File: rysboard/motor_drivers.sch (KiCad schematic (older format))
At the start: 30 parts, among them J2 Motor L, J3 Motor R, U1 L6470, U2 L6470, U5 74HC2G00

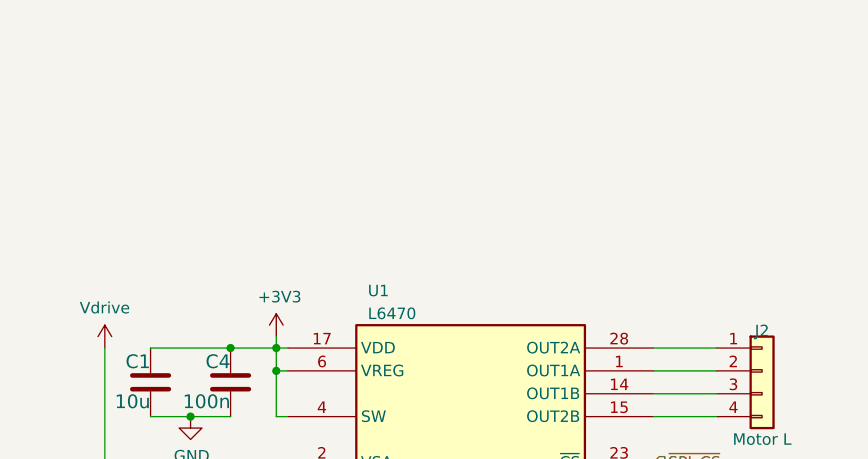
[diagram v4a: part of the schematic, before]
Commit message: first modyfications in St Motor section
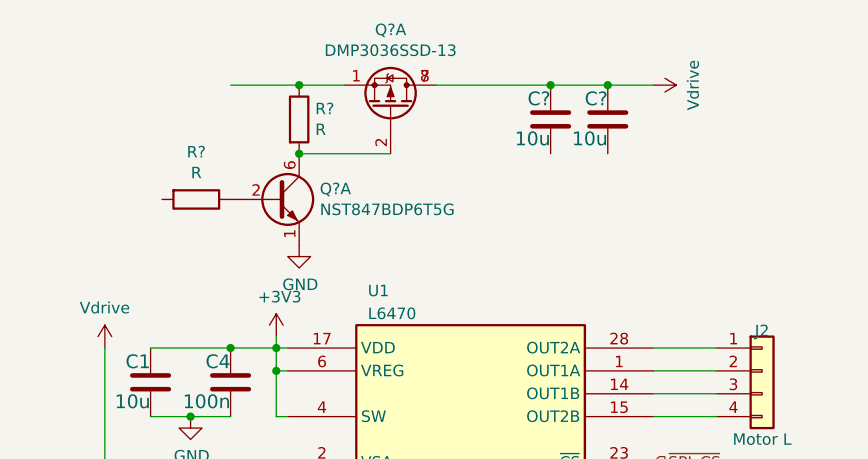
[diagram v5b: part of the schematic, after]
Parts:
- added C? (x2): 10u, Capacitor_SMD:C_1206_3216Metric, symbol Device:C
- added Q?: DMP3036SSD-13, Package_SO:SO-8_5.3x6.2mm_P1.27mm, symbol rysboard:DMP3036SSD-13
- added Q?: NST847BDP6T5G, Package_TO_SOT_SMD:SOT-963, symbol rysboard:NST847BDP6T5G
- added R? (x2): R, symbol Device:R
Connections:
- net GND: now also Q?.1 (E1)
- net Vdrive: now also C?.1, C?.1, Q?.7 (d), Q?.8 (d)
- new net: Q?.1 (S1), R?.1
- new net: Q?.2 (G1), Q?.6 (C1), R?.2
- new net: Q?.2 (B1), R?.1
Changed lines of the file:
@@
 	1    0    0    -1
 $EndComp
+$Comp
+L rysboard:DMP3036SSD-13 Q?
+U 1 1 603966B2
+P 2900 1050
+F 0 "Q?" V 3242 1050 50  0000 C CNN
+F 1 "DMP3036SSD-13" V 3151 1050 50  0000 C CNN
+F 2 "Package_SO:SO-8_5.3x6.2mm_P1.27mm" H 3100 975 50  0001 L CIN
+F 3 "http://www.vishay.com/docs/70209/70209.pdf" H 2900 1050 50  0001 L CNN
+	1    2900 1050
+	0    1    -1   0
+$EndComp
+$Comp
+L Device:C C?
+U 1 1 603970BA
+P 3600 1100
+F 0 "C?" H 3600 1225 60  0000 R TNN
+F 1 "10u" H 3600 1050 60  0000 R TNN
+F 2 "Capacitor_SMD:C_1206_3216Metric" H 3500 1190 60  0001 C CNN
+F 3 "" H 3500 1190 60  0000 C CNN
+	1    3600 1100
+	1    0    0    -1
+$EndComp
+$Comp
+L Device:C C?
+U 1 1 60397388
+P 3850 1100
+F 0 "C?" H 3850 1225 60  0000 R TNN
+F 1 "10u" H 3850 1050 60  0000 R TNN
+F 2 "Capacitor_SMD:C_1206_3216Metric" H 3750 1190 60  0001 C CNN
+F 3 "" H 3750 1190 60  0000 C CNN
+	1    3850 1100
+	1    0    0    -1
+$EndComp
+Wire Wire Line
+	3100 950  3600 950
+Connection ~ 3600 950
+Wire Wire Line
+	3600 950  3850 950
+$Comp
+L power:Vdrive #PWR?
+U 1 1 6039DE74
+P 4050 950
+F 0 "#PWR?" H 3850 800 50  0001 C CNN
+F 1 "Vdrive" H 4050 1125 50  0000 C CNN
+F 2 "" H 4050 950 50  0001 C CNN
+F 3 "" H 4050 950 50  0001 C CNN
+	1    4050 950
+	0    1    1    0
+$EndComp
+Wire Wire Line
+	4050 950  3850 950
+Connection ~ 3850 950
+$Comp
+L rysboard:NST847BDP6T5G Q?
+U 1 1 603A44DC
+P 2400 1450
+F 0 "Q?" H 2590 1496 50  0000 L CNN
+F 1 "NST847BDP6T5G" H 2590 1405 50  0000 L CNN
+F 2 "Package_TO_SOT_SMD:SOT-963" H 2600 1550 50  0001 C CNN
+F 3 "~" H 2400 1450 50  0001 C CNN
+	1    2400 1450
+	1    0    0    -1
+$EndComp
+$Comp
+L power:GND #PWR?
+U 1 1 603A5682
+P 2500 1650
+F 0 "#PWR?" H 2500 1400 50  0001 C CNN
+F 1 "GND" H 2505 1477 50  0000 C CNN
+F 2 "" H 2500 1650 50  0001 C CNN
+F 3 "" H 2500 1650 50  0001 C CNN
+	1    2500 1650
+	1    0    0    -1
+$EndComp
+Wire Wire Line
+	2500 1250 2900 1250
+$Comp
+L Device:R R?
+U 1 1 603AB9BC
+P 2500 1100
+F 0 "R?" H 2570 1146 50  0000 L CNN
+F 1 "R" H 2570 1055 50  0000 L CNN
+F 2 "" V 2430 1100 50  0001 C CNN
+F 3 "~" H 2500 1100 50  0001 C CNN
+	1    2500 1100
+	1    0    0    -1
+$EndComp
+Connection ~ 2500 1250
+Wire Wire Line
+	2700 950  2500 950
+Connection ~ 2500 950
+Wire Wire Line
+	2500 950  2200 950
+$Comp
+L Device:R R?
+U 1 1 603B1D08
+P 2050 1450
+F 0 "R?" V 1843 1450 50  0000 C CNN
+F 1 "R" V 1934 1450 50  0000 C CNN
+F 2 "" V 1980 1450 50  0001 C CNN
+F 3 "~" H 2050 1450 50  0001 C CNN
+	1    2050 1450
+	0    1    1    0
+$EndComp
 $EndSCHEMATC

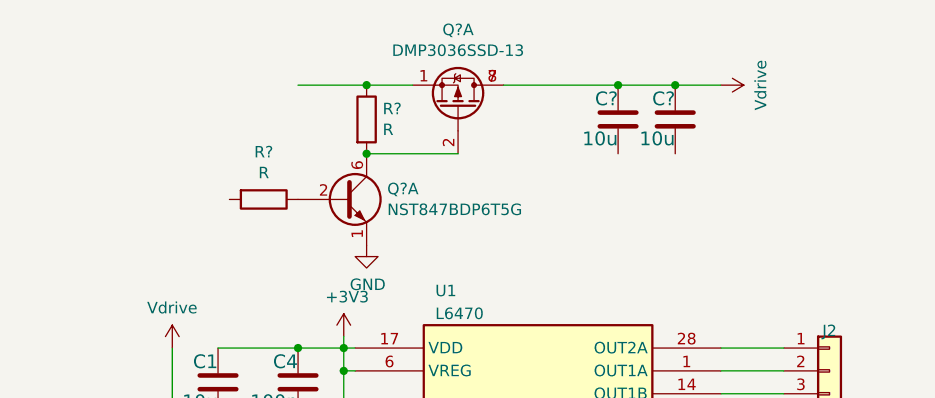
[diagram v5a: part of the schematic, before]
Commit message: Added eval board for STM32G031K8U6, rybsoard layout done, exact vals yet to be calculated
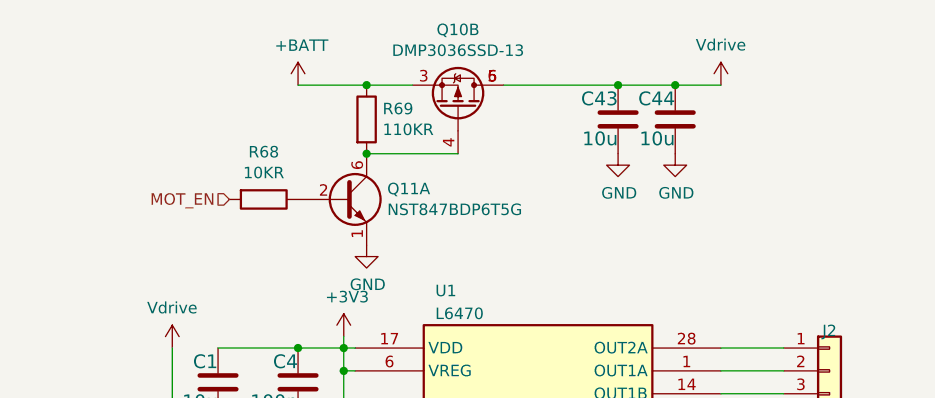
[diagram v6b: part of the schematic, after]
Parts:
- R68: renamed from R?; value R -> 10KR
- R69: renamed from R?; value R -> 110KR
- gave numbers to parts that had none: 4
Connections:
- net GND: now also C43.2, C44.2
- net Vdrive: now also Q10.5 (d), Q10.6 (d); no longer Q10.7 (d), Q10.8 (d)
- net +BATT: now reaches R69.1
- net +BATT: now also Q10.3 (S2); no longer Q10.1 (S1)
- net at Q11.6 (C1), R69.2: now also Q10.4 (G2); no longer Q10.2 (G1)
- net MOT_EN: now reaches R68.2
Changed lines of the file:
@@
 $Descr A4 11693 8268
 encoding utf-8
-Sheet 6 7
+Sheet 7 7
 Title "rysboard"
 Date "2020-08-23"
@@
 $EndComp
 $Comp
-L rysboard:DMP3036SSD-13 Q?
-U 1 1 603966B2
+L rysboard:DMP3036SSD-13 Q10
+U 2 1 603966B2
 P 2900 1050
-F 0 "Q?" V 3242 1050 50  0000 C CNN
+F 0 "Q10" V 3242 1050 50  0000 C CNN
 F 1 "DMP3036SSD-13" V 3151 1050 50  0000 C CNN
 F 2 "Package_SO:SO-8_5.3x6.2mm_P1.27mm" H 3100 975 50  0001 L CIN
 F 3 "http://www.vishay.com/docs/70209/70209.pdf" H 2900 1050 50  0001 L CNN
-	1    2900 1050
+	2    2900 1050
 	0    1    -1   0
 $EndComp
 $Comp
-L Device:C C?
+L Device:C C43
 U 1 1 603970BA
 P 3600 1100
-F 0 "C?" H 3600 1225 60  0000 R TNN
+F 0 "C43" H 3600 1225 60  0000 R TNN
 F 1 "10u" H 3600 1050 60  0000 R TNN
 F 2 "Capacitor_SMD:C_1206_3216Metric" H 3500 1190 60  0001 C CNN
@@
 $EndComp
 $Comp
-L Device:C C?
+L Device:C C44
 U 1 1 60397388
 P 3850 1100
-F 0 "C?" H 3850 1225 60  0000 R TNN
+F 0 "C44" H 3850 1225 60  0000 R TNN
 F 1 "10u" H 3850 1050 60  0000 R TNN
 F 2 "Capacitor_SMD:C_1206_3216Metric" H 3750 1190 60  0001 C CNN
@@
 	3600 950  3850 950
 $Comp
-L power:Vdrive #PWR?
+L power:Vdrive #PWR059
 U 1 1 6039DE74
 P 4050 950
-F 0 "#PWR?" H 3850 800 50  0001 C CNN
+F 0 "#PWR059" H 3850 800 50  0001 C CNN
 F 1 "Vdrive" H 4050 1125 50  0000 C CNN
 F 2 "" H 4050 950 50  0001 C CNN
 F 3 "" H 4050 950 50  0001 C CNN
 	1    4050 950
-	0    1    1    0
+	1    0    0    -1
 $EndComp
 Wire Wire Line
@@
 Connection ~ 3850 950
 $Comp
-L rysboard:NST847BDP6T5G Q?
+L rysboard:NST847BDP6T5G Q11
 U 1 1 603A44DC
 P 2400 1450
-F 0 "Q?" H 2590 1496 50  0000 L CNN
+F 0 "Q11" H 2590 1496 50  0000 L CNN
 F 1 "NST847BDP6T5G" H 2590 1405 50  0000 L CNN
 F 2 "Package_TO_SOT_SMD:SOT-963" H 2600 1550 50  0001 C CNN
@@
 $EndComp
 $Comp
-L power:GND #PWR?
+L power:GND #PWR058
 U 1 1 603A5682
 P 2500 1650
-F 0 "#PWR?" H 2500 1400 50  0001 C CNN
+F 0 "#PWR058" H 2500 1400 50  0001 C CNN
 F 1 "GND" H 2505 1477 50  0000 C CNN
 F 2 "" H 2500 1650 50  0001 C CNN
@@
 	2500 1250 2900 1250
 $Comp
-L Device:R R?
+L Device:R R69
 U 1 1 603AB9BC
 P 2500 1100
-F 0 "R?" H 2570 1146 50  0000 L CNN
-F 1 "R" H 2570 1055 50  0000 L CNN
+F 0 "R69" H 2570 1146 50  0000 L CNN
+F 1 "110KR" H 2570 1055 50  0000 L CNN
 F 2 "" V 2430 1100 50  0001 C CNN
 F 3 "~" H 2500 1100 50  0001 C CNN
@@
 	2500 950  2200 950
 $Comp
-L Device:R R?
+L Device:R R68
 U 1 1 603B1D08
 P 2050 1450
-F 0 "R?" V 1843 1450 50  0000 C CNN
-F 1 "R" V 1934 1450 50  0000 C CNN
+F 0 "R68" V 1843 1450 50  0000 C CNN
+F 1 "10KR" V 1934 1450 50  0000 C CNN
 F 2 "" V 1980 1450 50  0001 C CNN
 F 3 "~" H 2050 1450 50  0001 C CNN
@@
 	0    1    1    0
 $EndComp
+Text HLabel 1900 1450 0    50   Input ~ 0
+MOT_EN
+$Comp
+L power:+BATT #PWR?
+U 1 1 6042D379
+P 2200 950
+F 0 "#PWR?" H 2200 800 50  0001 C CNN
+F 1 "+BATT" H 2215 1123 50  0000 C CNN
+F 2 "" H 2200 950 50  0001 C CNN
+F 3 "" H 2200 950 50  0001 C CNN
+	1    2200 950
+	1    0    0    -1
+$EndComp
+$Comp
+L power:GND #PWR?
+U 1 1 6042EE06
+P 3600 1250
+F 0 "#PWR?" H 3600 1000 50  0001 C CNN
+F 1 "GND" H 3605 1077 50  0000 C CNN
+F 2 "" H 3600 1250 50  0001 C CNN
+F 3 "" H 3600 1250 50  0001 C CNN
+	1    3600 1250
+	1    0    0    -1
+$EndComp
+$Comp
+L power:GND #PWR?
+U 1 1 6042F02D
+P 3850 1250
+F 0 "#PWR?" H 3850 1000 50  0001 C CNN
+F 1 "GND" H 3855 1077 50  0000 C CNN
+F 2 "" H 3850 1250 50  0001 C CNN
+F 3 "" H 3850 1250 50  0001 C CNN
+	1    3850 1250
+	1    0    0    -1
+$EndComp
 $EndSCHEMATC

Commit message: new mosfet footprints
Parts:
- R68, R69: footprint (none) -> Resistor_SMD:R_0603_1608Metric
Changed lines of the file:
@@
 F 0 "R69" H 2570 1146 50  0000 L CNN
 F 1 "110KR" H 2570 1055 50  0000 L CNN
-F 2 "" V 2430 1100 50  0001 C CNN
+F 2 "Resistor_SMD:R_0603_1608Metric" V 2430 1100 50  0001 C CNN
 F 3 "~" H 2500 1100 50  0001 C CNN
 	1    2500 1100
@@
 F 0 "R68" V 1843 1450 50  0000 C CNN
 F 1 "10KR" V 1934 1450 50  0000 C CNN
-F 2 "" V 1980 1450 50  0001 C CNN
+F 2 "Resistor_SMD:R_0603_1608Metric" V 1980 1450 50  0001 C CNN
 F 3 "~" H 2050 1450 50  0001 C CNN
 	1    2050 1450
@@
 MOT_EN
 $Comp
-L power:+BATT #PWR?
+L power:+BATT #PWR062
 U 1 1 6042D379
 P 2200 950
-F 0 "#PWR?" H 2200 800 50  0001 C CNN
+F 0 "#PWR062" H 2200 800 50  0001 C CNN
 F 1 "+BATT" H 2215 1123 50  0000 C CNN
 F 2 "" H 2200 950 50  0001 C CNN
@@
 $EndComp
 $Comp
-L power:GND #PWR?
+L power:GND #PWR063
 U 1 1 6042EE06
 P 3600 1250
-F 0 "#PWR?" H 3600 1000 50  0001 C CNN
+F 0 "#PWR063" H 3600 1000 50  0001 C CNN
 F 1 "GND" H 3605 1077 50  0000 C CNN
 F 2 "" H 3600 1250 50  0001 C CNN
@@
 $EndComp
 $Comp
-L power:GND #PWR?
+L power:GND #PWR064
 U 1 1 6042F02D
 P 3850 1250
-F 0 "#PWR?" H 3850 1000 50  0001 C CNN
+F 0 "#PWR064" H 3850 1000 50  0001 C CNN
 F 1 "GND" H 3855 1077 50  0000 C CNN
 F 2 "" H 3850 1250 50  0001 C CNN

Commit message: Fixed library, added a few MOSFET layouts
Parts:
- removed Q10: DMP3036SSD-13, Package_SO:SO-8_5.3x6.2mm_P1.27mm, symbol rysboard:DMP3036SSD-13
- added Q8: DMP3036SSD-13, Package_SO:SO-8_3.9x4.9mm_P1.27mm, symbol rysboard:DMP3036SSD-13
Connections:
- net +BATT: now also Q8.3 (S2)
- net Vdrive: now also Q8.5 (d), Q8.6 (d)
- net at Q11.6 (C1), R69.2: now also Q8.4 (G2)
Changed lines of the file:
@@
 F 1 "27k1%" H 4475 3610 60  0000 L BNN
 F 2 "Resistor_SMD:R_0603_1608Metric" H 4335 3650 60  0001 C CNN
-F 3 "" H 4335 3650 60  0000 C CNN
+F 3 "~" H 4335 3650 60  0000 C CNN
 	1    4425 3700
 	1    0    0    -1
@@
 F 1 "47u" H 5325 3810 60  0000 L BNN
 F 2 "Capacitor_Tantalum_SMD:CP_EIA-7343-31_Kemet-D" H 5325 3810 60  0001 C CNN
-F 3 "" H 5325 3810 60  0000 C CNN
+F 3 "~" H 5325 3810 60  0000 C CNN
 	1    5225 3900
 	1    0    0    -1
@@
 F 1 "47u" H 4925 3810 60  0000 L BNN
 F 2 "Capacitor_Tantalum_SMD:CP_EIA-7343-31_Kemet-D" H 4925 3810 60  0001 C CNN
-F 3 "" H 4925 3810 60  0000 C CNN
+F 3 "~" H 4925 3810 60  0000 C CNN
 	1    4825 3900
 	1    0    0    -1
@@
 F 1 "100n" H 5700 3825 60  0000 L BNN
 F 2 "Capacitor_SMD:C_0603_1608Metric" H 5500 3990 60  0001 C CNN
-F 3 "" H 5500 3990 60  0001 C CNN
+F 3 "~" H 5500 3990 60  0001 C CNN
 	1    5600 3900
 	1    0    0    -1
@@
 F 1 "10k1%" H 4475 4010 60  0000 L BNN
 F 2 "Resistor_SMD:R_0603_1608Metric" H 4335 4050 60  0001 C CNN
-F 3 "" H 4335 4050 60  0000 C CNN
+F 3 "~" H 4335 4050 60  0000 C CNN
 	1    4425 4100
 	1    0    0    -1
@@
 F 1 "Motor L" H 4525 1900 50  0000 C CNN
 F 2 "Connector_Molex:Molex_Micro-Fit_3.0_43650-0415_1x04_P3.00mm_Vertical" H 4775 2350 50  0001 C CNN
-F 3 "" H 4775 2350 50  0001 C CNN
+F 3 "~" H 4775 2350 50  0001 C CNN
 	1    4525 2200
 	1    0    0    -1
@@
 F 1 "220n" V 1925 2675 60  0000 L BNN
 F 2 "Capacitor_SMD:C_0805_2012Metric" H 2150 2840 60  0001 C CNN
-F 3 "" H 2150 2840 60  0000 C CNN
+F 3 "~" H 2150 2840 60  0000 C CNN
 	1    1950 2950
 	0    -1   -1   0
@@
 F 1 "40k" H 1525 6035 60  0000 L BNN
 F 2 "Resistor_SMD:R_0603_1608Metric" H 1385 6075 60  0001 C CNN
-F 3 "" H 1385 6075 60  0000 C CNN
+F 3 "~" H 1385 6075 60  0000 C CNN
 	1    1475 6125
 	1    0    0    -1
@@
 F 1 "40k" H 1825 6035 60  0000 L BNN
 F 2 "Resistor_SMD:R_0603_1608Metric" H 1685 6075 60  0001 C CNN
-F 3 "" H 1685 6075 60  0000 C CNN
+F 3 "~" H 1685 6075 60  0000 C CNN
 	1    1775 6125
 	1    0    0    -1
@@
 F 1 "10u" H 1850 2200 60  0000 R TNN
 F 2 "Capacitor_SMD:C_1206_3216Metric" H 1750 2340 60  0001 C CNN
-F 3 "" H 1750 2340 60  0000 C CNN
+F 3 "~" H 1750 2340 60  0000 C CNN
 	1    1850 2250
 	1    0    0    -1
@@
 F 1 "100n" H 2200 2200 60  0000 R TNN
 F 2 "Capacitor_SMD:C_0603_1608Metric" H 2100 2340 60  0001 C CNN
-F 3 "" H 2100 2340 60  0001 C CNN
+F 3 "~" H 2100 2340 60  0001 C CNN
 	1    2200 2250
 	1    0    0    -1
@@
 F 1 "27k1%" H 8975 3610 60  0000 L BNN
 F 2 "Resistor_SMD:R_0603_1608Metric" H 8835 3650 60  0001 C CNN
-F 3 "" H 8835 3650 60  0000 C CNN
+F 3 "~" H 8835 3650 60  0000 C CNN
 	1    8925 3700
 	1    0    0    -1
@@
 F 1 "47u" H 9825 3810 60  0000 L BNN
 F 2 "Capacitor_Tantalum_SMD:CP_EIA-7343-31_Kemet-D" H 9825 3810 60  0001 C CNN
-F 3 "" H 9825 3810 60  0000 C CNN
+F 3 "~" H 9825 3810 60  0000 C CNN
 	1    9725 3900
 	1    0    0    -1
@@
 F 1 "47u" H 9425 3810 60  0000 L BNN
 F 2 "Capacitor_Tantalum_SMD:CP_EIA-7343-31_Kemet-D" H 9425 3810 60  0001 C CNN
-F 3 "" H 9425 3810 60  0000 C CNN
+F 3 "~" H 9425 3810 60  0000 C CNN
 	1    9325 3900
 	1    0    0    -1
@@
 F 1 "100n" H 10200 3825 60  0000 L BNN
 F 2 "Capacitor_SMD:C_0603_1608Metric" H 10000 3990 60  0001 C CNN
-F 3 "" H 10000 3990 60  0001 C CNN
+F 3 "~" H 10000 3990 60  0001 C CNN
 	1    10100 3900
 	1    0    0    -1
@@
 F 1 "10k1%" H 8975 4010 60  0000 L BNN
 F 2 "Resistor_SMD:R_0603_1608Metric" H 8835 4050 60  0001 C CNN
-F 3 "" H 8835 4050 60  0000 C CNN
+F 3 "~" H 8835 4050 60  0000 C CNN
 	1    8925 4100
 	1    0    0    -1
@@
 F 1 "Motor R" H 9025 1900 50  0000 C CNN
 F 2 "Connector_Molex:Molex_Micro-Fit_3.0_43650-0415_1x04_P3.00mm_Vertical" H 9275 2350 50  0001 C CNN
-F 3 "" H 9275 2350 50  0001 C CNN
+F 3 "~" H 9275 2350 50  0001 C CNN
 	1    9025 2200
 	1    0    0    -1
@@
 F 1 "220n" V 6425 2675 60  0000 L BNN
 F 2 "Capacitor_SMD:C_0805_2012Metric" H 6650 2840 60  0001 C CNN
-F 3 "" H 6650 2840 60  0000 C CNN
+F 3 "~" H 6650 2840 60  0000 C CNN
 	1    6450 2950
 	0    -1   -1   0
@@
 F 1 "10u" H 6350 2200 60  0000 R TNN
 F 2 "Capacitor_SMD:C_1206_3216Metric" H 6250 2340 60  0001 C CNN
-F 3 "" H 6250 2340 60  0000 C CNN
+F 3 "~" H 6250 2340 60  0000 C CNN
 	1    6350 2250
 	1    0    0    -1
@@
 F 1 "100n" H 6700 2200 60  0000 R TNN
 F 2 "Capacitor_SMD:C_0603_1608Metric" H 6600 2340 60  0001 C CNN
-F 3 "" H 6600 2340 60  0001 C CNN
+F 3 "~" H 6600 2340 60  0001 C CNN
 	1    6700 2250
 	1    0    0    -1
@@
 F 1 "40k" H 2125 6035 60  0000 L BNN
 F 2 "Resistor_SMD:R_0603_1608Metric" H 1985 6075 60  0001 C CNN
-F 3 "" H 1985 6075 60  0000 C CNN
+F 3 "~" H 1985 6075 60  0000 C CNN
 	1    2075 6125
 	1    0    0    -1
@@
 F 1 "40k" H 2425 6035 60  0000 L BNN
 F 2 "Resistor_SMD:R_0603_1608Metric" H 2285 6075 60  0001 C CNN
-F 3 "" H 2285 6075 60  0000 C CNN
+F 3 "~" H 2285 6075 60  0000 C CNN
 	1    2375 6125
 	1    0    0    -1
@@
 F 1 "40k" H 2725 6035 60  0000 L BNN
 F 2 "Resistor_SMD:R_0603_1608Metric" H 2585 6075 60  0001 C CNN
-F 3 "" H 2585 6075 60  0000 C CNN
+F 3 "~" H 2585 6075 60  0000 C CNN
 	1    2675 6125
 	1    0    0    -1
@@
 $EndComp
 $Comp
-L rysboard:DMP3036SSD-13 Q10
-U 2 1 603966B2
-P 2900 1050
-F 0 "Q10" V 3242 1050 50  0000 C CNN
-F 1 "DMP3036SSD-13" V 3151 1050 50  0000 C CNN
-F 2 "Package_SO:SO-8_5.3x6.2mm_P1.27mm" H 3100 975 50  0001 L CIN
-F 3 "http://www.vishay.com/docs/70209/70209.pdf" H 2900 1050 50  0001 L CNN
-	2    2900 1050
-	0    1    -1   0
-$EndComp
-$Comp
 L Device:C C43
 U 1 1 603970BA
@@
 F 1 "10u" H 3600 1050 60  0000 R TNN
 F 2 "Capacitor_SMD:C_1206_3216Metric" H 3500 1190 60  0001 C CNN
-F 3 "" H 3500 1190 60  0000 C CNN
+F 3 "~" H 3500 1190 60  0000 C CNN
 	1    3600 1100
 	1    0    0    -1
@@
 F 1 "10u" H 3850 1050 60  0000 R TNN
 F 2 "Capacitor_SMD:C_1206_3216Metric" H 3750 1190 60  0001 C CNN
-F 3 "" H 3750 1190 60  0000 C CNN
+F 3 "~" H 3750 1190 60  0000 C CNN
 	1    3850 1100
 	1    0    0    -1
@@
 	1    0    0    -1
 $EndComp
+$Comp
+L rysboard:DMP3036SSD-13 Q8
+U 2 1 6053F608
+P 2900 1050
+F 0 "Q8" V 3242 1050 50  0000 C CNN
+F 1 "DMP3036SSD-13" V 3151 1050 50  0000 C CNN
+F 2 "Package_SO:SO-8_3.9x4.9mm_P1.27mm" H 3100 975 50  0001 L CIN
+F 3 "" H 2900 1050 50  0001 L CNN
+	2    2900 1050
+	0    1    -1   0
+$EndComp
 $EndSCHEMATC
